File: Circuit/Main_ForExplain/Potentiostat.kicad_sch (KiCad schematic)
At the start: 29 parts, among them U1 ${SIM.PARAMS}, U10 ${SIM.PARAMS}, U2 ${SIM.PARAMS}, U3 ${SIM.PARAMS}, U8 ${SIM.PARAMS}, U9 ${SIM.PARAMS}

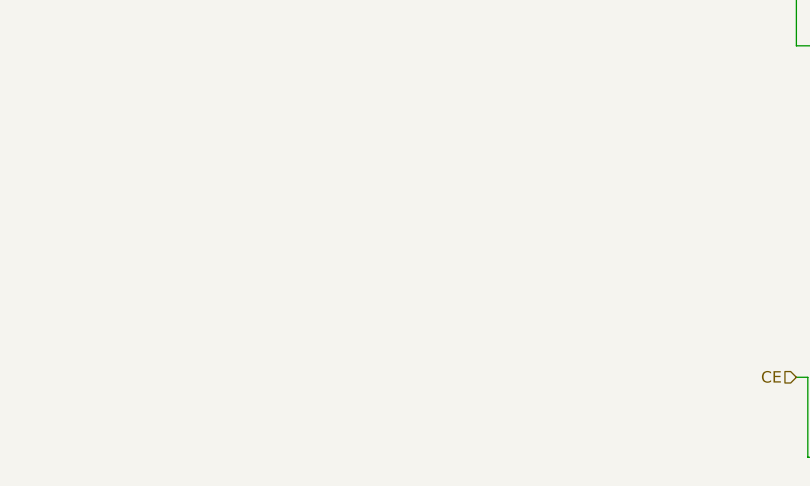
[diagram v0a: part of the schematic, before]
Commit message: ケースを更新
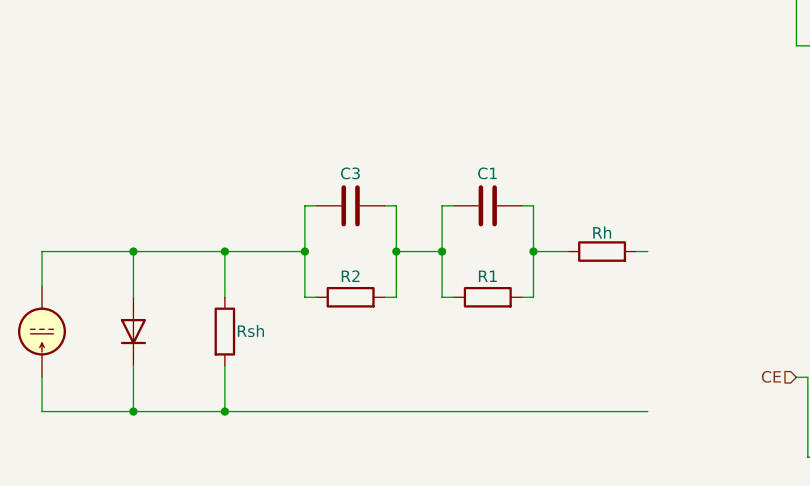
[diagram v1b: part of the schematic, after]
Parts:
- added C11: C3, symbol Device:C
- added C12: C1, symbol Device:C
- added D1: D, symbol Device:D
- added I1: 1, symbol Simulation_SPICE:IDC
- added R22: Rsh, symbol Device:R
- added R25: R2, symbol Device:R
- added R26: R1, symbol Device:R
- added R27: Rh, symbol Device:R
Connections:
- new net: D1.1 (K), I1.1, R22.2
- new net: C11.1, D1.2 (A), I1.2, R22.1, R25.1
- new net: C12.2, R26.2, R27.1
- new net: C11.2, C12.1, R25.2, R26.1
